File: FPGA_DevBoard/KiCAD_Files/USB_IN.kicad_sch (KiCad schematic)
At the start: 33 parts, among them J14 AWHW 14G-SMD, J3 USB4105-GF-A-060, SW1 219-8MST, U12 FT4232HPQ-REEL, X2 12MHz

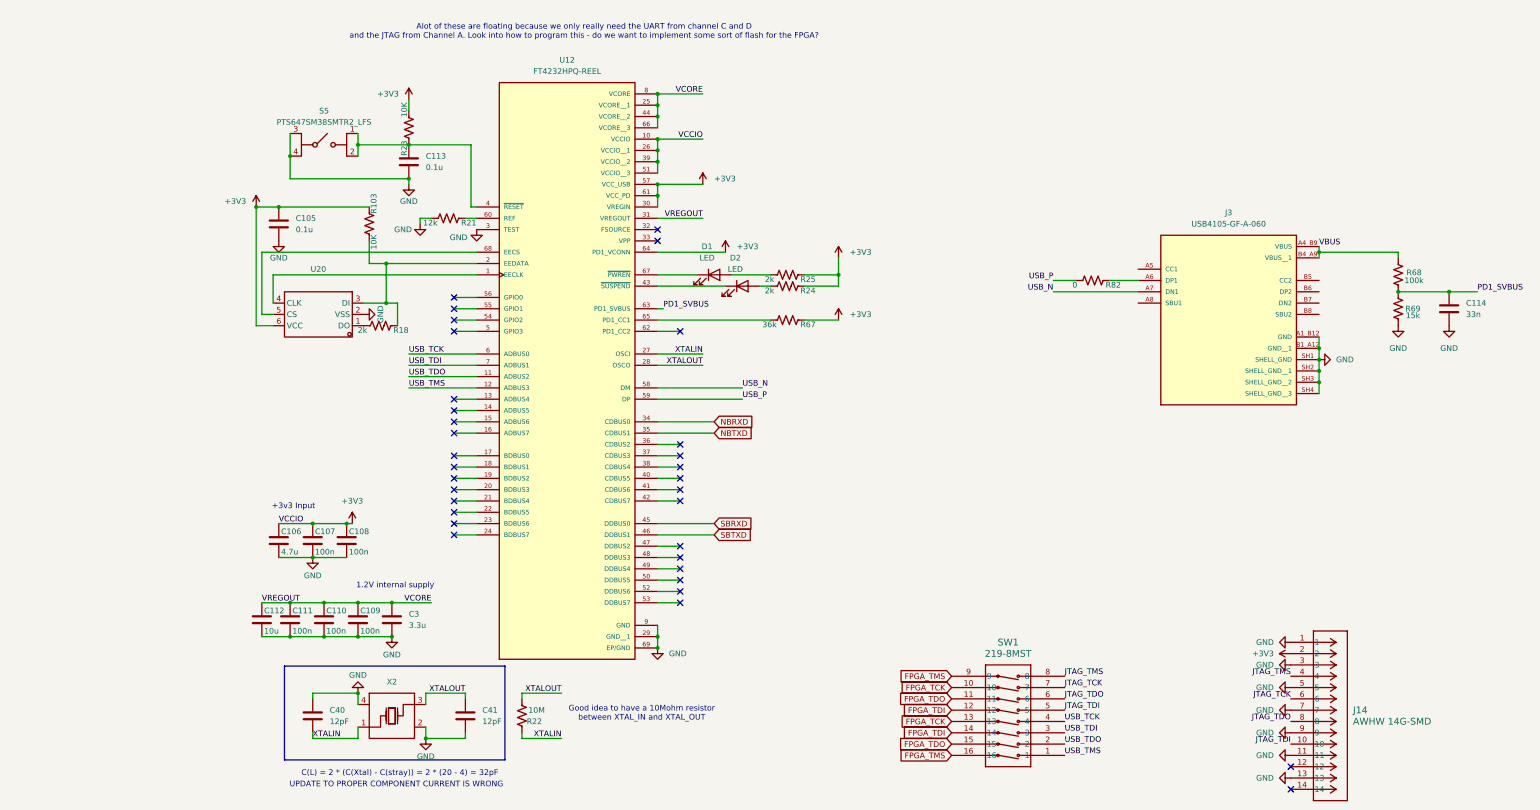
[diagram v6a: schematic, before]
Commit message: Updated the layout to remove the JTAG header, connect the proper lines for the UART, and connect the proper pins for the audio.
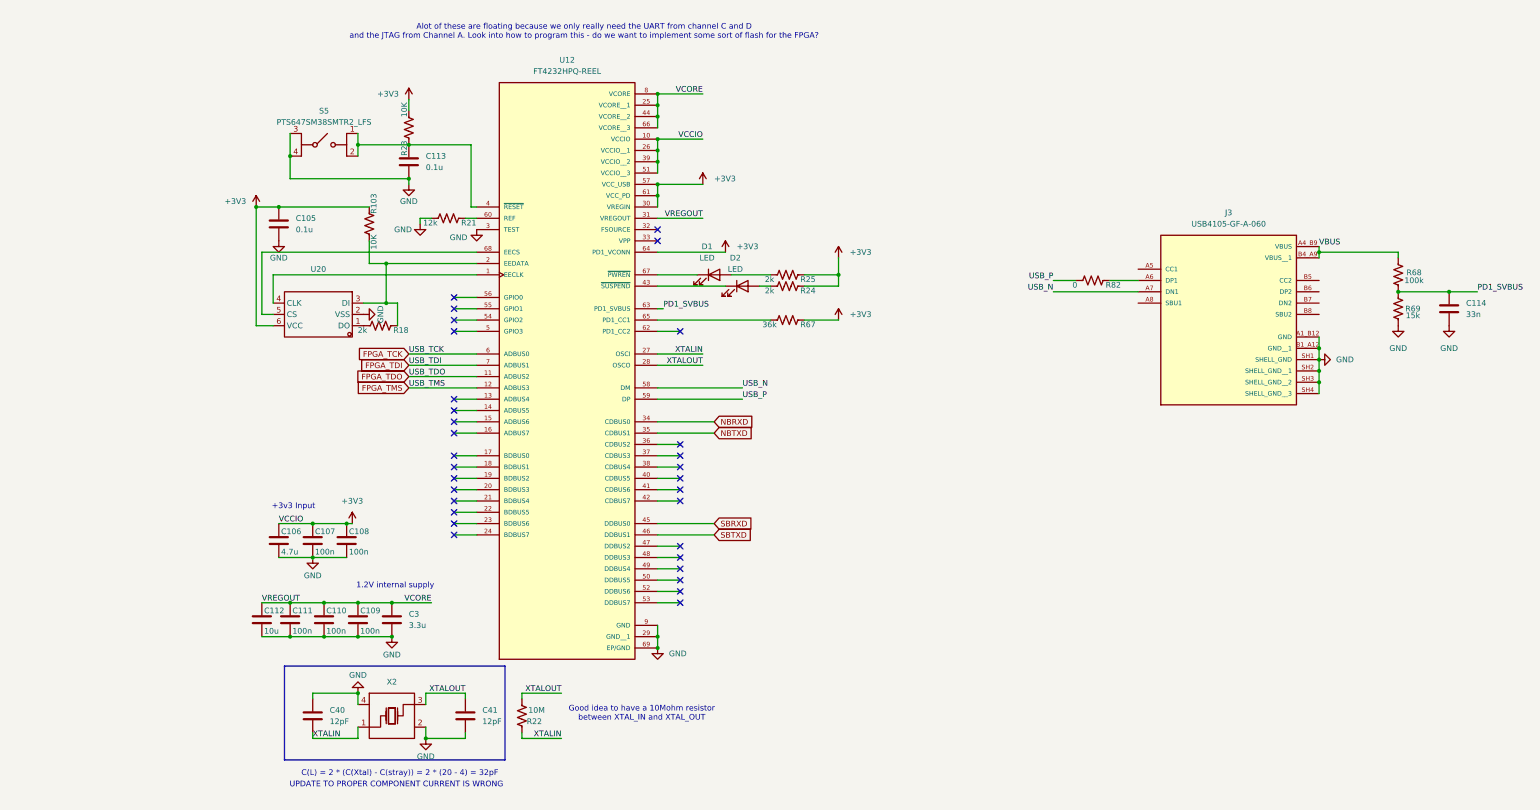
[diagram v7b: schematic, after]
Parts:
- removed J14: AWHW 14G-SMD, FPGA_Interface:CONN_AWHW 14G-SMD_ASM, symbol FPGA_Interface:AWHW_14G-SMD
- removed SW1: 219-8MST, FPGA_Interface:219-8M, symbol 219_8MST:219-8MST
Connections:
- net USB_TCK is gone; now on net FPGA_TCK: U12.6 (ADBUS0)
- net USB_TDI is gone; now on net FPGA_TDI: U12.7 (ADBUS1)
- net USB_TDO is gone; now on net FPGA_TDO: U12.11 (ADBUS2)
- net USB_TMS is gone; now on net FPGA_TMS: U12.12 (ADBUS3)
- no-connect marks 33 -> 31

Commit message: This is V2 Ordered
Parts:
- removed R82: 0, Resistor_SMD:R_0402_1005Metric, symbol Device:R_US
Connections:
- net USB_P: now also J3.A6 (DP1)
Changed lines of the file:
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@@
 	(wire
 		(pts
-			(xy 247.65 78.74) (xy 254 78.74)
-		)
-		(stroke
-			(width 0)
-			(type default)
-		)
-	)
-	(wire
-		(pts
 			(xy 146.05 125.73) (xy 151.13 125.73)
 		)
@@
 	(wire
 		(pts
-			(xy 234.95 78.74) (xy 240.03 78.74)
+			(xy 234.95 78.74) (xy 254 78.74)
 		)
 		(stroke
@@
 					(unit 1)
 				)
-			)
-		)
-	)
-	(symbol
-		(lib_id "Device:R_US")
-		(at 243.84 78.74 270)
-		(unit 1)
-		(body_style 1)
-		(exclude_from_sim no)
-		(in_bom yes)
-		(on_board yes)
-		(in_pos_files yes)
-		(dnp no)
-		(property "Reference" "R82"
-			(at 248.412 79.756 90)
-			(show_name no)
-			(do_not_autoplace no)
-			(effects
-				(font
-					(size 1.27 1.27)
-				)
-			)
-		)
-		(property "Value" "0"
-			(at 239.776 79.756 90)
-			(show_name no)
-			(do_not_autoplace no)
-			(effects
-				(font
-					(size 1.27 1.27)
-				)
-			)
-		)
-		(property "Footprint" "Resistor_SMD:R_0402_1005Metric"
-			(at 243.586 79.756 90)
-			(hide yes)
-			(show_name no)
-			(do_not_autoplace no)
-			(effects
-				(font
-					(size 1.27 1.27)
-				)
-			)
-		)
-		(property "Datasheet" ""
-			(at 243.84 78.74 0)
-			(hide yes)
-			(show_name no)
-			(do_not_autoplace no)
-			(effects
-				(font
-					(size 1.27 1.27)
-				)
-			)
-		)
-		(property "Description" "Resistor, US symbol"
-			(at 243.84 78.74 0)
-			(hide yes)
-			(show_name no)
-			(do_not_autoplace no)
-			(effects
-				(font
-					(size 1.27 1.27)
-				)
-			)
-		)
-		(pin "1"
-		)
-		(pin "2"
-		)
-		(instances
-			(project "FPGA_DevBoard"
-				(path "/29dacc10-fb0d-42da-8b4b-fe903faf3f1a/0234104c-5c7a-412d-afd7-9cfe7478c407"
-					(reference "R82")
-					(unit 1)
-				)
